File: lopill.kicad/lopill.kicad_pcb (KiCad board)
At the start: 2 copper layers, 23 x 59.5 mm, 34 parts, among them J1 Pins Left, J2 SWD, J3 USB_B_Micro, J4 Pins Right, SW1 RESET, U1 XC6206PxxxMR, U2 STM32L052C8Tx, Y1 8MHz, Y2 32.768KHz

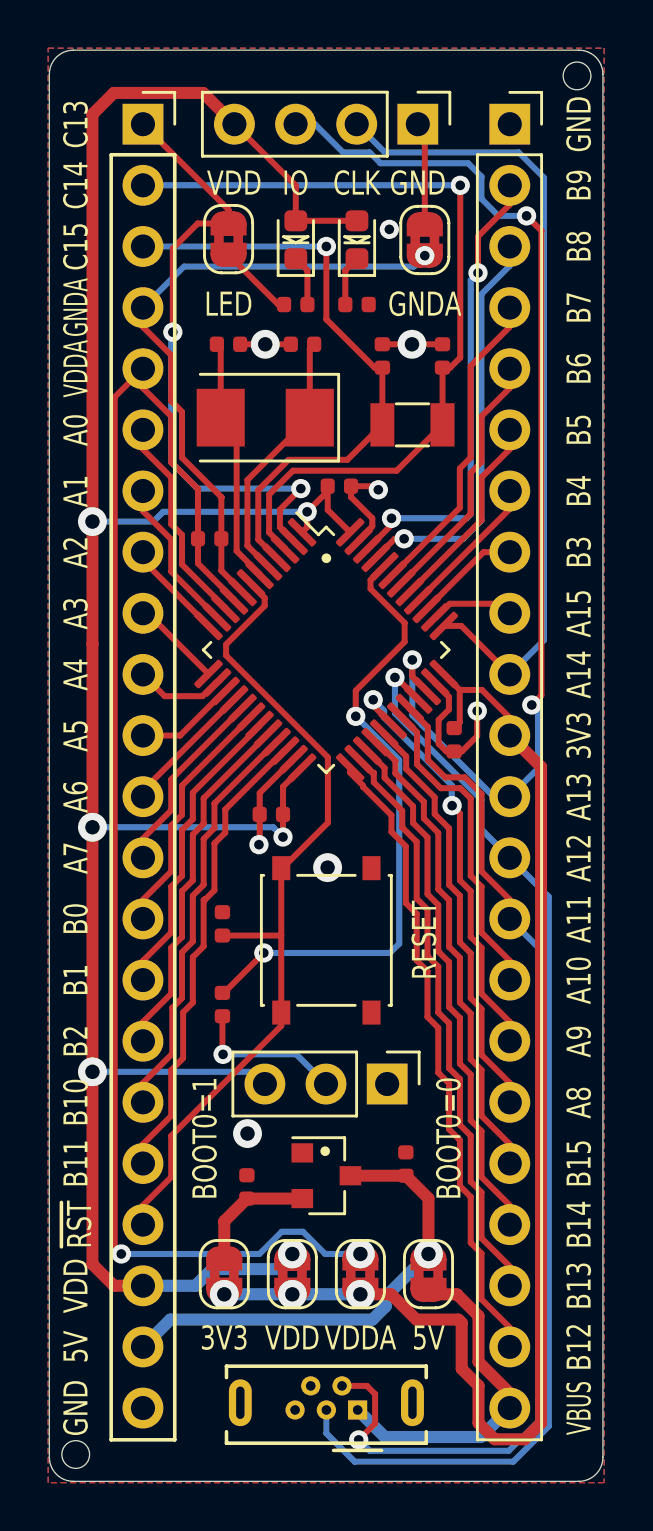
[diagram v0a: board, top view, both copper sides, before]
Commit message: Add 3D model of 8MHz crystal
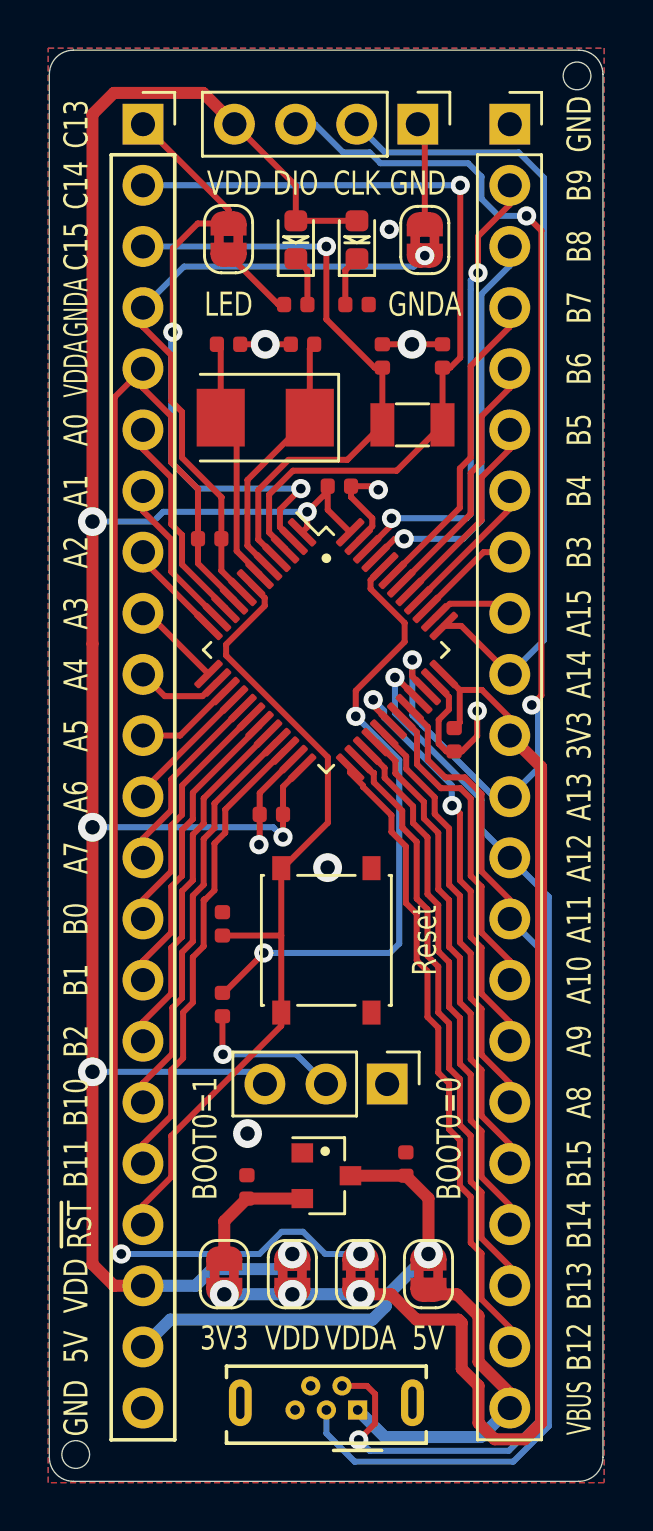
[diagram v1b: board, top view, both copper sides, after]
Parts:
- SW1: value RESET -> Reset
- Y1: footprint Crystal:Crystal_SMD_5032-2Pin_5.0x3.2mm -> lopill:Crystal_SMD_5032-2Pin_5.0x3.2mm_YXC
